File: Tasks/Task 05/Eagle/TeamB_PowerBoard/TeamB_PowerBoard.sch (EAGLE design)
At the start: 35 parts, among them X1 5566-2, X2 5566-2, X3 C-GRID-02-70543, X4 C-GRID-02-70543, X5 C-GRID-02-70543, X6 C-GRID-02-70543

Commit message: Added PCB Layout
ERC passes for both PCB and Schematic layouts!
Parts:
- 12VOUT: value C-GRID-02-70543 -> LIDAR
- 3.3VOUT: value C-GRID-02-70543 -> CPU
- 5VOUT: value C-GRID-02-70543 -> ENCODER
- 5VOUT2: value C-GRID-02-70543 -> Wi-Fi
- renumbered LED1 to 3.3_LED, LED2 to 5.0_LED, LED3 to 12_LED, U$4 to D1, U$5 to D2, U$6 to D3, U$7 to D4, X1 to 24VIN, X2 to 24VOUT, X3 to 12VOUT, X4 to 5VOUT2, X5 to 5VOUT, X6 to 3.3VOUT
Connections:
- new net N$6: C4.2, R5.1, U$2.GND
- net GND: no longer C4.2, R5.1, U$2.GND

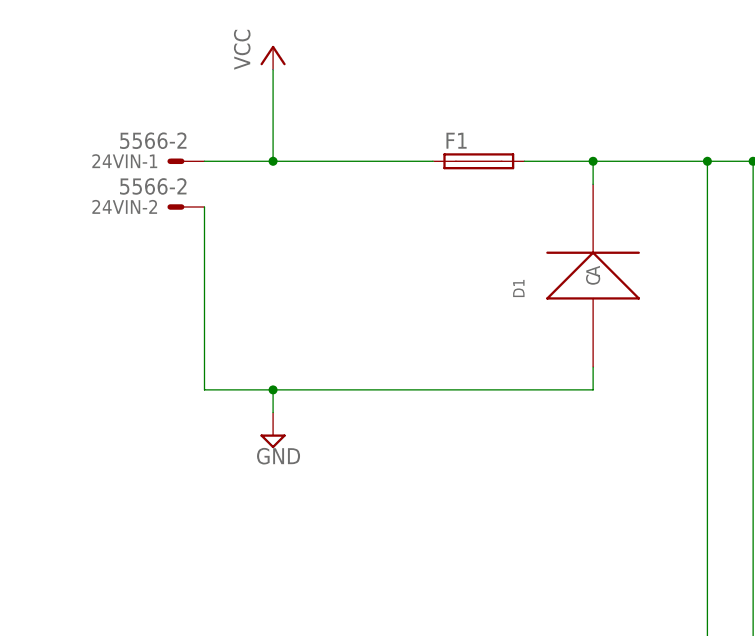
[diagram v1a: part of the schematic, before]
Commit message: Added 4th LED
Added 4th LED to PCB and Schematic
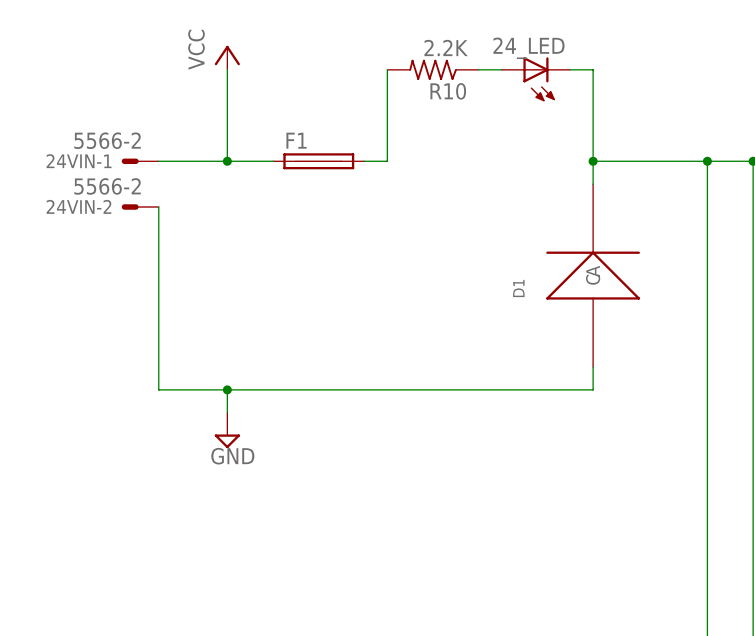
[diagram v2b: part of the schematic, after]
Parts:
- added 24_LED: (no value), led:LEDSML1206
- added R10: 2.2K, rcl:R-US_R1206
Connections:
- new net N$10: F1.2, R10.2
- new net N$20: 24_LED.A, R10.1
- net N$1: now also 24_LED.C; no longer F1.2
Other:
- moved on the sheet: 24VIN-1, 24VIN-2, F1
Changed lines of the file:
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@@
 <part name="SUPPLY14" library="supply2" deviceset="GND" device=""/>
 <part name="SUPPLY15" library="supply2" deviceset="GND" device=""/>
+<part name="R10" library="rcl" deviceset="R-US_" device="R1206" value="2.2K"/>
+<part name="24_LED" library="led" deviceset="LED" device="SML1206"/>
 </parts>
 <sheets>
@@
 </plain>
 <instances>
-<instance part="24VIN" gate="-1" x="-5.08" y="157.48" rot="MR0"/>
-<instance part="24VIN" gate="-2" x="-5.08" y="152.4" rot="MR0"/>
+<instance part="24VIN" gate="-1" x="-10.16" y="157.48" rot="MR0"/>
+<instance part="24VIN" gate="-2" x="-10.16" y="152.4" rot="MR0"/>
 <instance part="24VOUT" gate="-1" x="226.06" y="157.48"/>
 <instance part="24VOUT" gate="-2" x="226.06" y="152.4"/>
@@
 <instance part="3.3VOUT" gate="-2" x="226.06" y="132.08"/>
 <instance part="3.3VOUT" gate="-1" x="226.06" y="134.62"/>
-<instance part="F1" gate="1" x="27.94" y="157.48"/>
+<instance part="F1" gate="1" x="10.16" y="157.48"/>
 <instance part="F2" gate="1" x="160.02" y="137.16"/>
 <instance part="F3" gate="1" x="160.02" y="93.98"/>
@@
 <instance part="5.0_LED" gate="G$1" x="187.96" y="93.98" rot="R90"/>
 <instance part="12_LED" gate="G$1" x="187.96" y="48.26" rot="R90"/>
-<instance part="SUPPLY1" gate="GND" x="5.08" y="127"/>
+<instance part="SUPPLY1" gate="GND" x="0" y="127"/>
 <instance part="SUPPLY2" gate="GND" x="104.14" y="109.22"/>
 <instance part="SUPPLY3" gate="GND" x="104.14" y="66.04"/>
@@
 <instance part="SUPPLY7" gate="GND" x="170.18" y="17.78"/>
 <instance part="SUPPLY8" gate="GND" x="210.82" y="144.78"/>
-<instance part="P+1" gate="VCC" x="5.08" y="170.18"/>
+<instance part="P+1" gate="VCC" x="0" y="170.18"/>
 <instance part="SUPPLY9" gate="GND" x="63.5" y="116.84"/>
 <instance part="SUPPLY10" gate="GND" x="63.5" y="71.12"/>
@@
 <instance part="SUPPLY14" gate="GND" x="220.98" y="71.12"/>
 <instance part="SUPPLY15" gate="GND" x="220.98" y="38.1"/>
+<instance part="R10" gate="G$1" x="22.86" y="167.64" rot="R180"/>
+<instance part="24_LED" gate="G$1" x="33.02" y="167.64" rot="R90"/>
 </instances>
 <busses>
@@
 <segment>
 <pinref part="P+1" gate="VCC" pin="VCC"/>
-<wire x1="5.08" y1="167.64" x2="5.08" y2="157.48" width="0.1524" layer="91"/>
+<wire x1="0" y1="167.64" x2="0" y2="157.48" width="0.1524" layer="91"/>
 <pinref part="24VIN" gate="-1" pin="S"/>
-<wire x1="5.08" y1="157.48" x2="-2.54" y2="157.48" width="0.1524" layer="91"/>
+<wire x1="0" y1="157.48" x2="-7.62" y2="157.48" width="0.1524" layer="91"/>
 <pinref part="F1" gate="1" pin="1"/>
-<wire x1="5.08" y1="157.48" x2="22.86" y2="157.48" width="0.1524" layer="91"/>
-<junction x="5.08" y="157.48"/>
+<wire x1="0" y1="157.48" x2="5.08" y2="157.48" width="0.1524" layer="91"/>
+<junction x="0" y="157.48"/>
 </segment>
 </net>
 <net name="N$1" class="0">
 <segment>
-<pinref part="F1" gate="1" pin="2"/>
 <pinref part="D1" gate="G$1" pin="C"/>
-<wire x1="33.02" y1="157.48" x2="40.64" y2="157.48" width="0.1524" layer="91"/>
 <wire x1="40.64" y1="157.48" x2="40.64" y2="154.94" width="0.1524" layer="91"/>
 <wire x1="40.64" y1="157.48" x2="53.34" y2="157.48" width="0.1524" layer="91"/>
-<junction x="40.64" y="157.48"/>
-<pinref part="24VOUT" gate="-1" pin="S"/>
 <pinref part="C1" gate="G$1" pin="1"/>
 <wire x1="53.34" y1="157.48" x2="58.42" y2="157.48" width="0.1524" layer="91"/>
 <wire x1="58.42" y1="157.48" x2="63.5" y2="157.48" width="0.1524" layer="91"/>
-<wire x1="63.5" y1="157.48" x2="223.52" y2="157.48" width="0.1524" layer="91"/>
 <wire x1="63.5" y1="137.16" x2="63.5" y2="142.24" width="0.1524" layer="91"/>
-<junction x="63.5" y="157.48"/>
 <pinref part="U$1" gate="G$1" pin="VIN"/>
 <wire x1="63.5" y1="142.24" x2="63.5" y2="157.48" width="0.1524" layer="91"/>
@@
 <wire x1="76.2" y1="38.1" x2="76.2" y2="58.42" width="0.1524" layer="91"/>
 <junction x="76.2" y="58.42"/>
+<pinref part="24_LED" gate="G$1" pin="C"/>
+<wire x1="38.1" y1="167.64" x2="40.64" y2="167.64" width="0.1524" layer="91"/>
+<wire x1="40.64" y1="167.64" x2="40.64" y2="157.48" width="0.1524" layer="91"/>
+<junction x="40.64" y="157.48"/>
+<pinref part="24VOUT" gate="-1" pin="S"/>
+<wire x1="63.5" y1="157.48" x2="223.52" y2="157.48" width="0.1524" layer="91"/>
+<junction x="63.5" y="157.48"/>
 </segment>
 </net>
@@
 <wire x1="40.64" y1="134.62" x2="40.64" y2="132.08" width="0.1524" layer="91"/>
 <pinref part="SUPPLY1" gate="GND" pin="GND"/>
-<wire x1="40.64" y1="132.08" x2="5.08" y2="132.08" width="0.1524" layer="91"/>
-<wire x1="5.08" y1="132.08" x2="5.08" y2="129.54" width="0.1524" layer="91"/>
+<wire x1="40.64" y1="132.08" x2="0" y2="132.08" width="0.1524" layer="91"/>
+<wire x1="0" y1="132.08" x2="0" y2="129.54" width="0.1524" layer="91"/>
 <pinref part="24VIN" gate="-2" pin="S"/>
-<wire x1="5.08" y1="132.08" x2="-2.54" y2="132.08" width="0.1524" layer="91"/>
-<wire x1="-2.54" y1="132.08" x2="-2.54" y2="152.4" width="0.1524" layer="91"/>
-<junction x="5.08" y="132.08"/>
+<wire x1="0" y1="132.08" x2="-7.62" y2="132.08" width="0.1524" layer="91"/>
+<wire x1="-7.62" y1="132.08" x2="-7.62" y2="152.4" width="0.1524" layer="91"/>
+<junction x="0" y="132.08"/>
 </segment>
 <segment>
@@
 </segment>
 </net>
+<net name="N$10" class="0">
+<segment>
+<pinref part="F1" gate="1" pin="2"/>
+<pinref part="R10" gate="G$1" pin="2"/>
+<wire x1="15.24" y1="157.48" x2="17.78" y2="157.48" width="0.1524" layer="91"/>
+<wire x1="17.78" y1="157.48" x2="17.78" y2="167.64" width="0.1524" layer="91"/>
+</segment>
+</net>
+<net name="N$20" class="0">
+<segment>
+<pinref part="R10" gate="G$1" pin="1"/>
+<pinref part="24_LED" gate="G$1" pin="A"/>
+<wire x1="27.94" y1="167.64" x2="30.48" y2="167.64" width="0.1524" layer="91"/>
+</segment>
+</net>

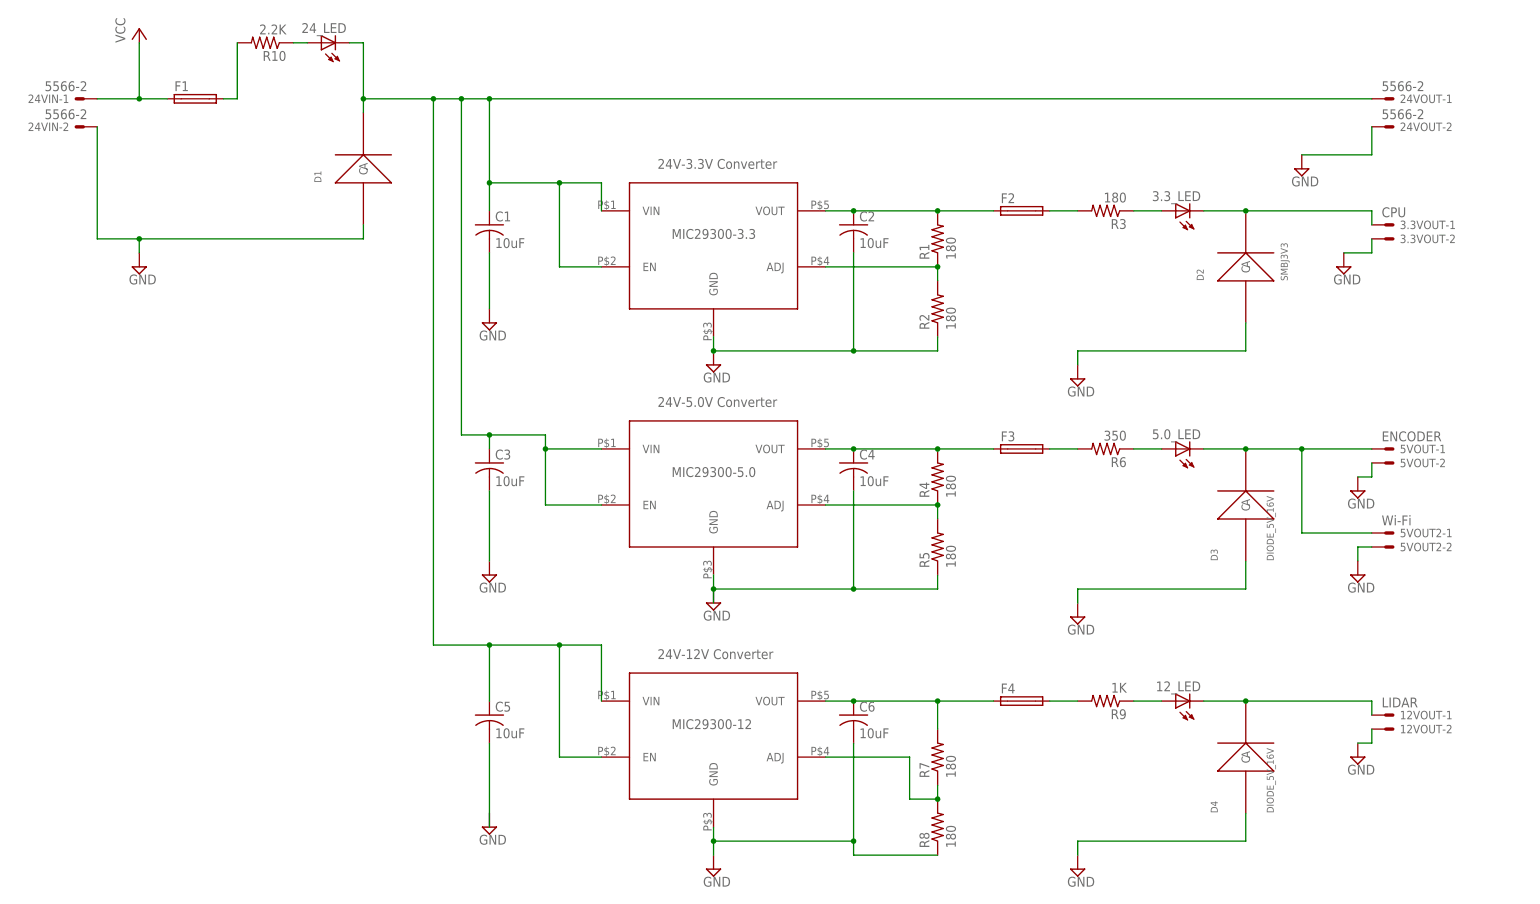
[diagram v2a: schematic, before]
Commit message: Fixed Libraries and Wiring
Fixed the Library components to reflect DIP variants.
Fixed schematic for LED wiring.
ERC passes for both PCB and SCH
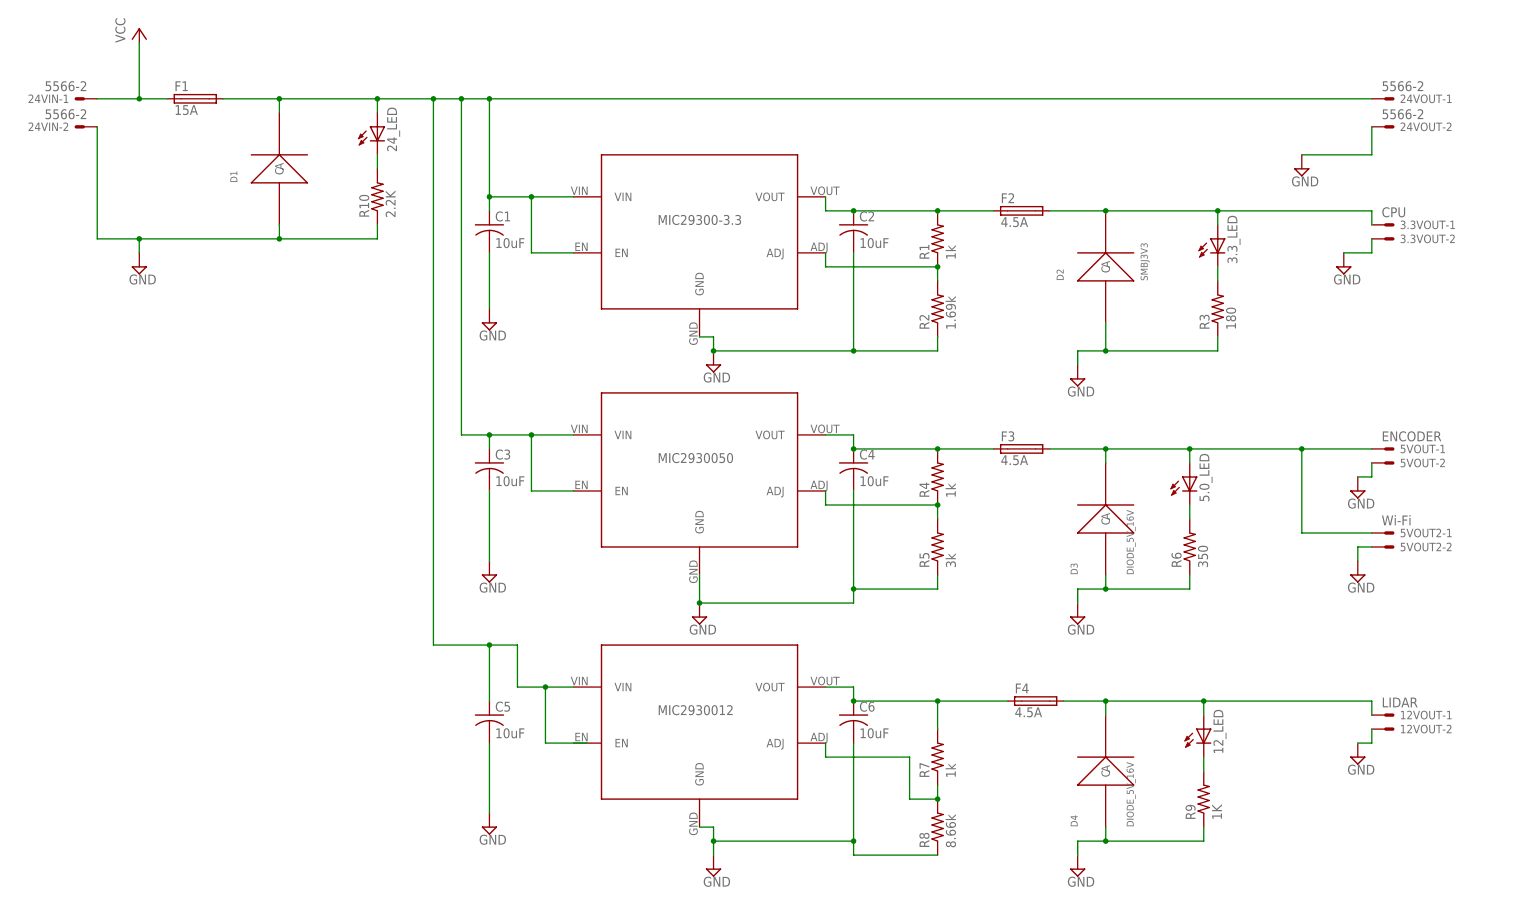
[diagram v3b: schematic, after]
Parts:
- F1: value (none) -> 15A
- F2, F3, F4: value (none) -> 4.5A
- R1, R4, R7: value 180 -> 1k
- R2: value 180 -> 1.69k
- R5: value 180 -> 3k
- R8: value 180 -> 8.66k
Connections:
- removed net N$14: 5.0_LED.A, R6.1
- removed net N$15: 5.0_LED.C, 5VOUT-1.S, 5VOUT2-1.S, D3.C
- removed net N$16: F4.2, R9.2
- removed net N$17: 12_LED.A, R9.1
- removed net N$18: 12VOUT-1.S, 12_LED.C, D4.C
- removed net N$20: 24_LED.A, R10.1
- net GND: now also C4.2, C5.2, R10.1, R3.1, R5.1, R6.1, R9.1, U$2.GND
- net N$1: now also 24_LED.A, F1.2; no longer 24_LED.C, U$3.EN
- net N$10: now also 12_LED.C, R9.2; no longer F1.2, R10.2
- net N$11: now also 3.3_LED.C, R3.2; no longer F3.2, R6.2
- net N$2: now also 5.0_LED.C, R6.2; no longer C5.2
- net N$3: now also 24_LED.C, R10.2; no longer F2.2, R3.2
- net N$4: now also 5.0_LED.A, 5VOUT-1.S, 5VOUT2-1.S, D3.C, F3.2; no longer 3.3_LED.A, R3.1
- net N$6: now also 12VOUT-1.S, 12_LED.A, D4.C, F4.2; no longer C4.2, R5.1, U$2.GND
- net N$9: now also 3.3_LED.A, F2.2; no longer 3.3_LED.C
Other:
- moved on the sheet: 12_LED, 24_LED, 3.3_LED, 5.0_LED, D1, D2, D3, D4, F4, R10, R3, R6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
